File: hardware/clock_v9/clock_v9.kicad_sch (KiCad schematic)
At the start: 173 parts, among them J1 RJ45, J12 Conn_01x06, J14 DC-063-25A, J2 Conn_01x06_Pin, J4 USB_C_Receptacle, J5 Conn_01x06_Pin, J6 Conn_01x04_Pin, J8 Conn_01x02, Q1 2N7002, Q10 2N7002, Q2 S8550, Q3 S8050, Q4 S8050, Q5 S8050, Q9 2N7002, SW1 LC1258OASP, U1 ADA4807-1, U10 STM32F405RGTx, U11 AMS1117-3.3, U12 BA50DD0WHFP-TR, U13 M24C02-RMN, U14 CH340C, U15 USBLC6-2P6, U16 TLV3603DCKR, U17 SN74LVC1G14DBV, U2 SN74LVC1G14DBV, U3 SN74LVC1G14DBV, U4 ADA4807-1, U5 ADA4807-1, U6 TLV3603DCKR, U7 SN74LVC1G14DBV, U8 TLV3603DCKR, U9 L78L05_SOT89, Y1 AOCJY4A-10.000MHZ-SW, Y2 16MHz

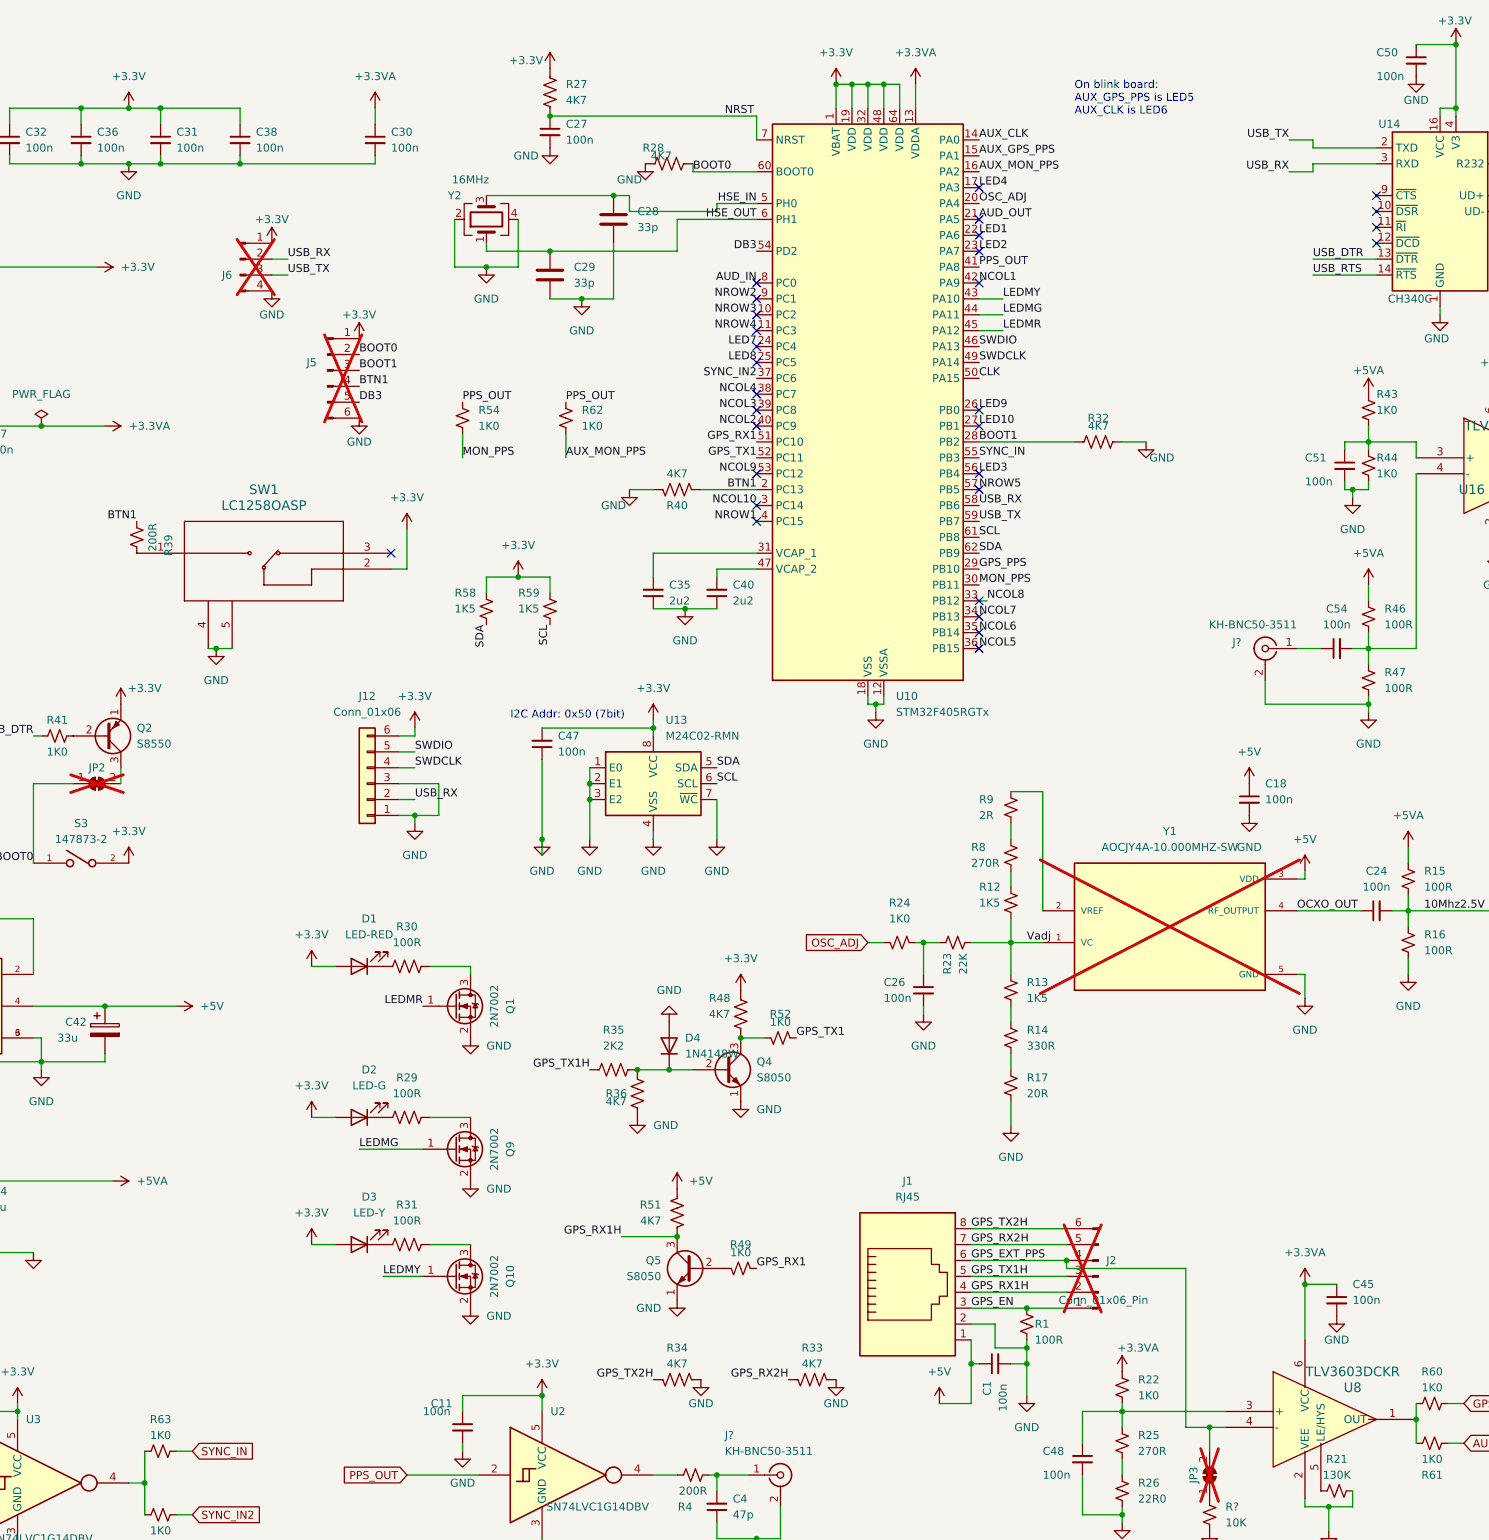
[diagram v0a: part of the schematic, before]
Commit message: add protection on inputs flips to outputs
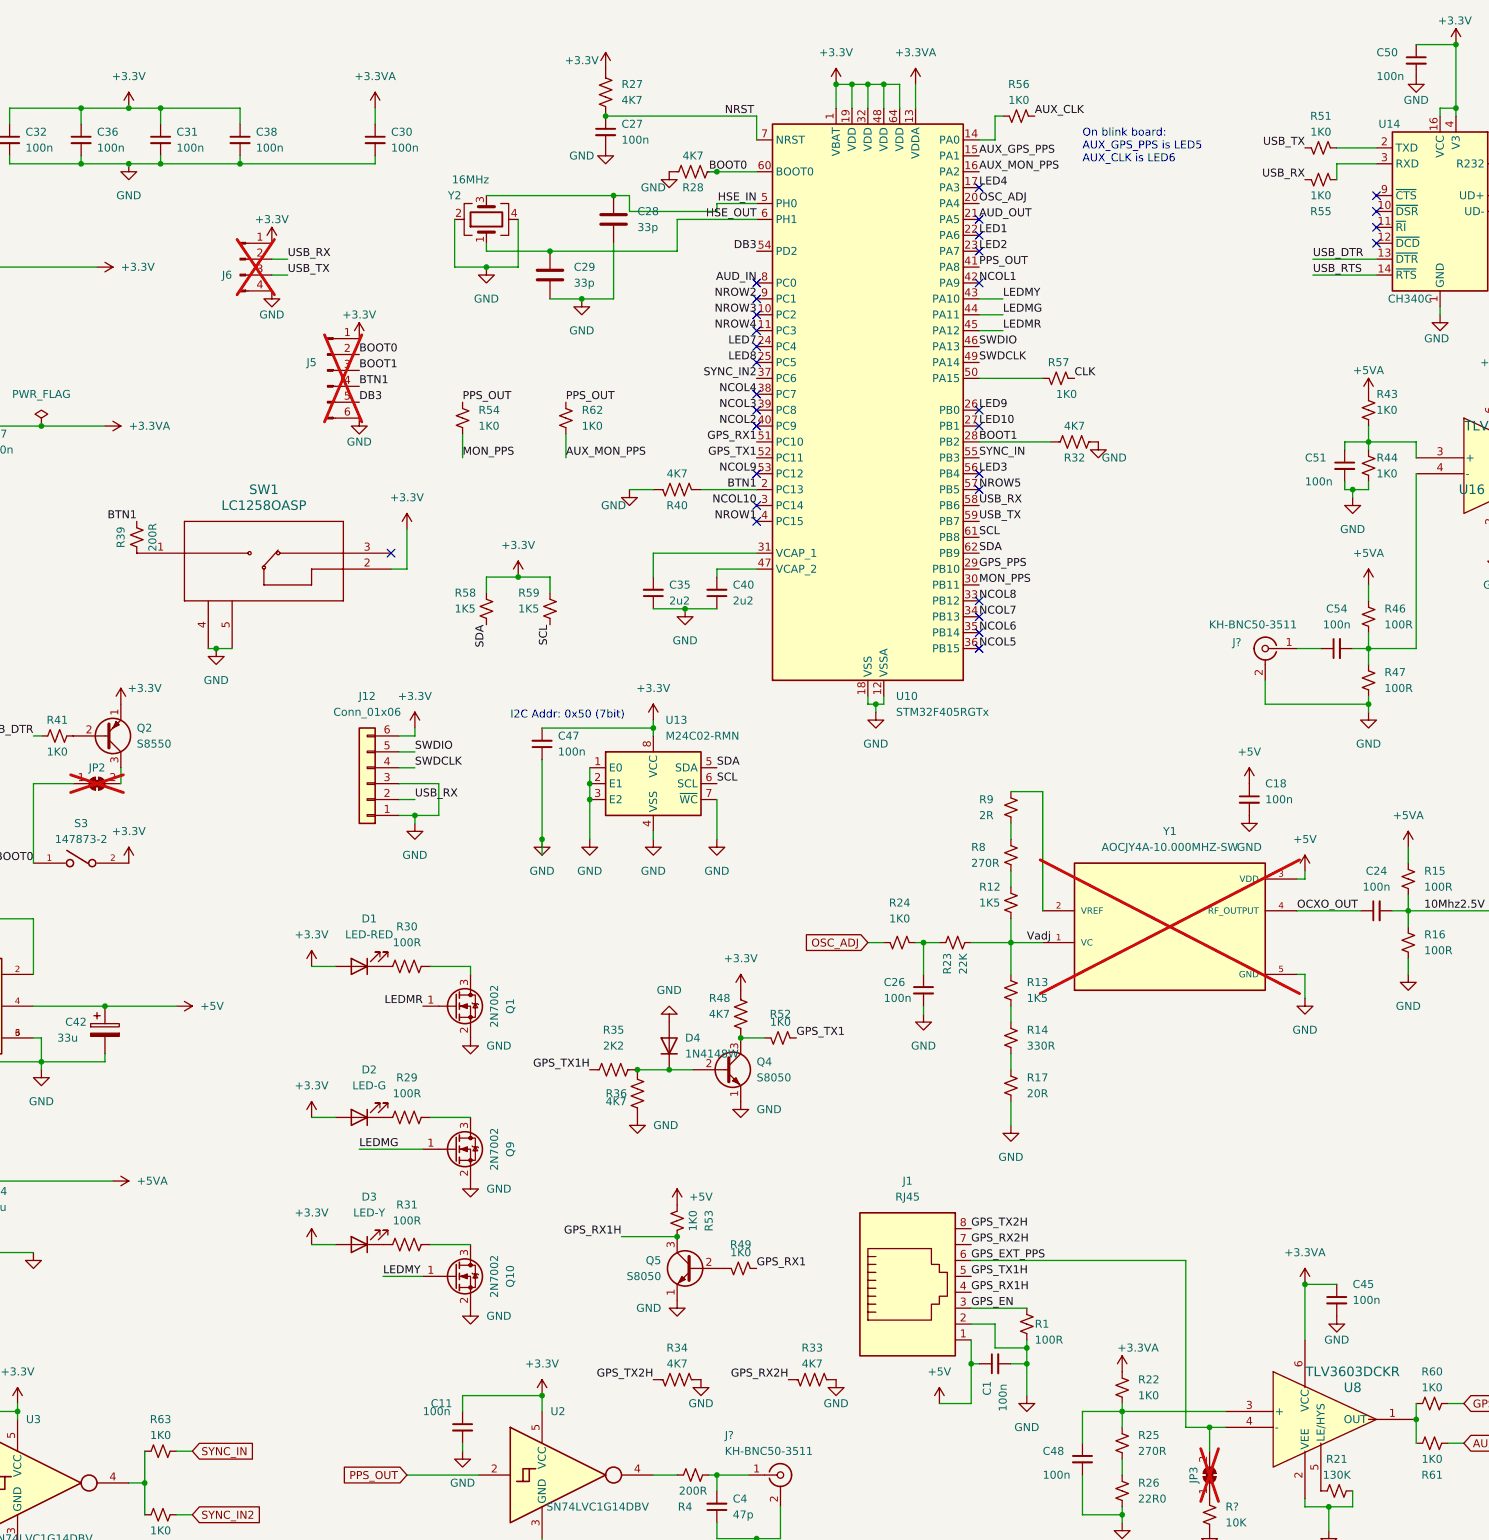
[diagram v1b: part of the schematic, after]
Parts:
- removed J2: Conn_01x06_Pin, Connector_PinHeader_2.54mm:PinHeader_1x06_P2.54mm_Vertical, symbol Connector:Conn_01x06_Pin
- removed R51: 4K7, Resistor_SMD:R_0603_1608Metric, symbol Device:R_US
- added R51, R53, R55, R56, R57: 1K0, Resistor_SMD:R_0603_1608Metric, symbol Device:R_Small_US
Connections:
- net +5V: now also R53.2
- net AUX_CLK: now also R56.1; no longer U10.14 (PA0)
- net CLK: now also R57.1; no longer U10.50 (PA15)
- net GPS_RX1H: now also R53.1
- net USB_RX: now also R55.1; no longer U14.3 (RXD)
- net USB_TX: now also R51.2; no longer U14.2 (TXD)
- new net: R56.2, U10.14 (PA0)
- new net: R57.2, U10.50 (PA15)
- new net: R51.1, U14.2 (TXD)
- new net: R55.2, U14.3 (RXD)
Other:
- moved on the sheet: C27, R27, R28, R32

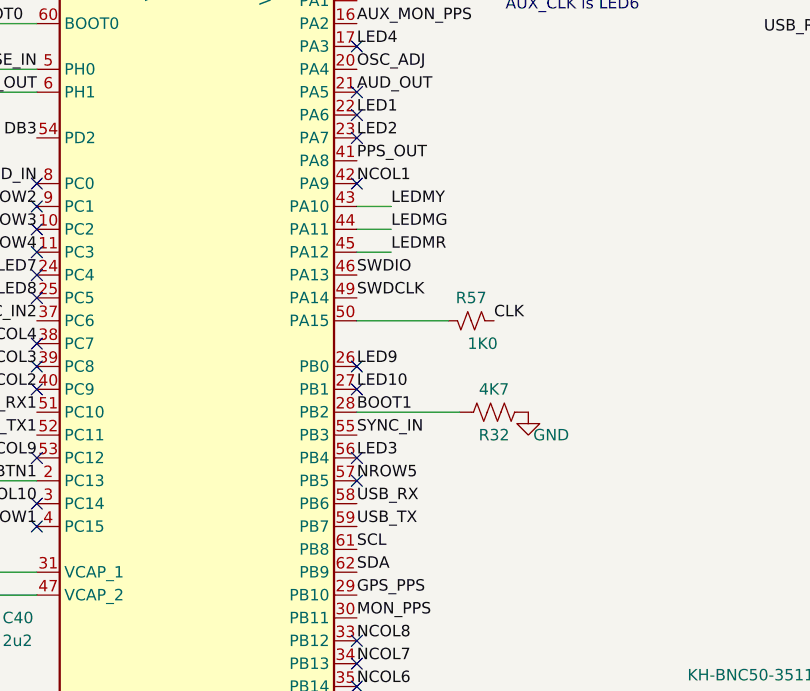
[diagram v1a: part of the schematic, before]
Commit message: move usb rx/tx on clock
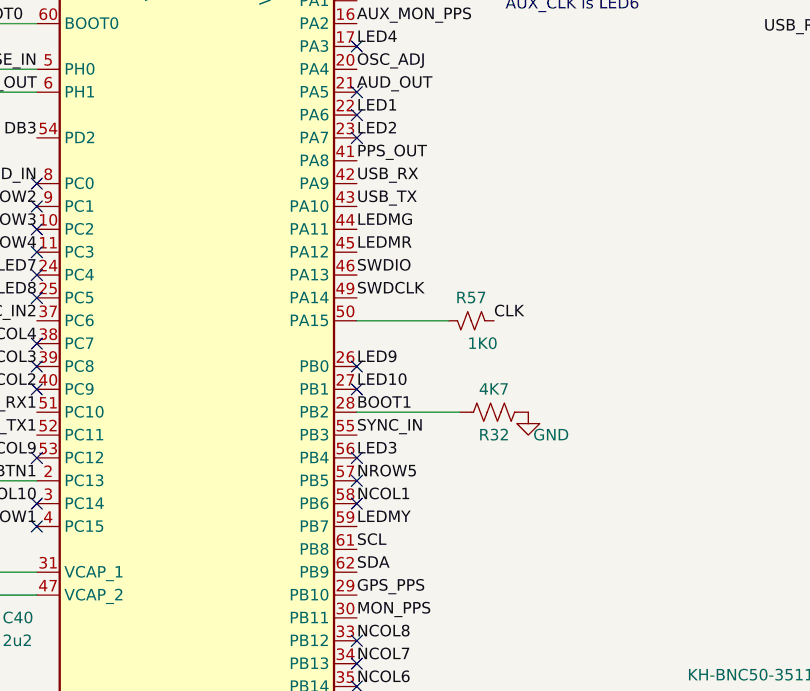
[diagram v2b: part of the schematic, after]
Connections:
- net LEDMY: now also U10.59 (PB7); no longer U10.43 (PA10)
- net NCOL1: now also U10.58 (PB6); no longer U10.42 (PA9)
- net USB_RX: now also U10.42 (PA9); no longer U10.58 (PB6)
- net USB_TX: now also U10.43 (PA10); no longer U10.59 (PB7)
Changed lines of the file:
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@@
   (no_connect (at 213.36 86.36))
   (no_connect (at 38.1 105.41))
+  (no_connect (at 213.36 91.44))
   (no_connect (at 410.21 31.75))
   (no_connect (at 276.86 44.45))
@@
   (no_connect (at 213.36 111.76))
   (no_connect (at 297.18 36.83))
-  (no_connect (at 213.36 55.88))
   (no_connect (at 177.8 93.98))
   (no_connect (at 177.8 55.88))
@@
     (stroke (width 0) (type default))
   )
-  (wire (pts (xy 217.17 60.96) (xy 213.36 60.96))
-    (stroke (width 0) (type default))
-  )
   (wire (pts (xy 69.85 27.94) (xy 77.47 27.94))
     (stroke (width 0) (type default))
@@
     (stroke (width 0) (type default))
   )
-  (wire (pts (xy 217.17 63.5) (xy 213.36 63.5))
-    (stroke (width 0) (type default))
-  )
   (wire (pts (xy 134.62 53.34) (xy 139.7 53.34))
     (stroke (width 0) (type default))
@@
   )
   (wire (pts (xy 198.12 24.13) (xy 198.12 27.94))
-    (stroke (width 0) (type default))
-  )
-  (wire (pts (xy 217.17 58.42) (xy 213.36 58.42))
     (stroke (width 0) (type default))
   )
@@
     (effects (font (size 1.27 1.27)) (justify left bottom))
   )
+  (label "LEDMY" (at 213.36 93.98 0) (fields_autoplaced)
+    (effects (font (size 1.27 1.27)) (justify left bottom))
+  )
   (label "GPS_RX1H" (at 156.21 208.28 180) (fields_autoplaced)
     (effects (font (size 1.27 1.27)) (justify right bottom))
@@
     (effects (font (size 1.27 1.27)) (justify right bottom))
   )
-  (label "LEDMY" (at 217.17 58.42 0) (fields_autoplaced)
-    (effects (font (size 1.27 1.27)) (justify left bottom))
-  )
   (label "GPS_RX2H" (at 182.88 231.14 180) (fields_autoplaced)
     (effects (font (size 1.27 1.27)) (justify right bottom))
@@
     (effects (font (size 1.27 1.27)) (justify left bottom))
   )
-  (label "LEDMR" (at 217.17 63.5 0) (fields_autoplaced)
+  (label "LEDMR" (at 213.36 63.5 0) (fields_autoplaced)
     (effects (font (size 1.27 1.27)) (justify left bottom))
   )
@@
     (effects (font (size 1.27 1.27)) (justify left bottom))
   )
-  (label "USB_TX" (at 213.36 93.98 0) (fields_autoplaced)
+  (label "USB_TX" (at 213.36 58.42 0) (fields_autoplaced)
     (effects (font (size 1.27 1.27)) (justify left bottom))
   )
@@
     (effects (font (size 1.27 1.27)) (justify left bottom))
   )
+  (label "NCOL1" (at 213.36 91.44 0) (fields_autoplaced)
+    (effects (font (size 1.27 1.27)) (justify left bottom))
+  )
   (label "NCOL5" (at 213.36 114.3 0) (fields_autoplaced)
     (effects (font (size 1.27 1.27)) (justify left bottom))
@@
     (effects (font (size 1.27 1.27)) (justify left bottom))
   )
-  (label "LEDMG" (at 217.17 60.96 0) (fields_autoplaced)
+  (label "LEDMG" (at 213.36 60.96 0) (fields_autoplaced)
     (effects (font (size 1.27 1.27)) (justify left bottom))
   )
@@
     (effects (font (size 1.27 1.27)) (justify left bottom))
   )
-  (label "USB_RX" (at 213.36 91.44 0) (fields_autoplaced)
-    (effects (font (size 1.27 1.27)) (justify left bottom))
-  )
   (label "AUD_IN" (at 177.8 55.88 180) (fields_autoplaced)
     (effects (font (size 1.27 1.27)) (justify right bottom))
@@
     (effects (font (size 1.27 1.27)) (justify left bottom))
   )
-  (label "NCOL1" (at 213.36 55.88 0) (fields_autoplaced)
-    (effects (font (size 1.27 1.27)) (justify left bottom))
-  )
   (label "SWDCLK" (at 123.19 133.35 0) (fields_autoplaced)
     (effects (font (size 1.27 1.27)) (justify left bottom))
@@
     (effects (font (size 1.27 1.27)) (justify left bottom))
   )
+  (label "USB_RX" (at 213.36 55.88 0) (fields_autoplaced)
+    (effects (font (size 1.27 1.27)) (justify left bottom))
+  )

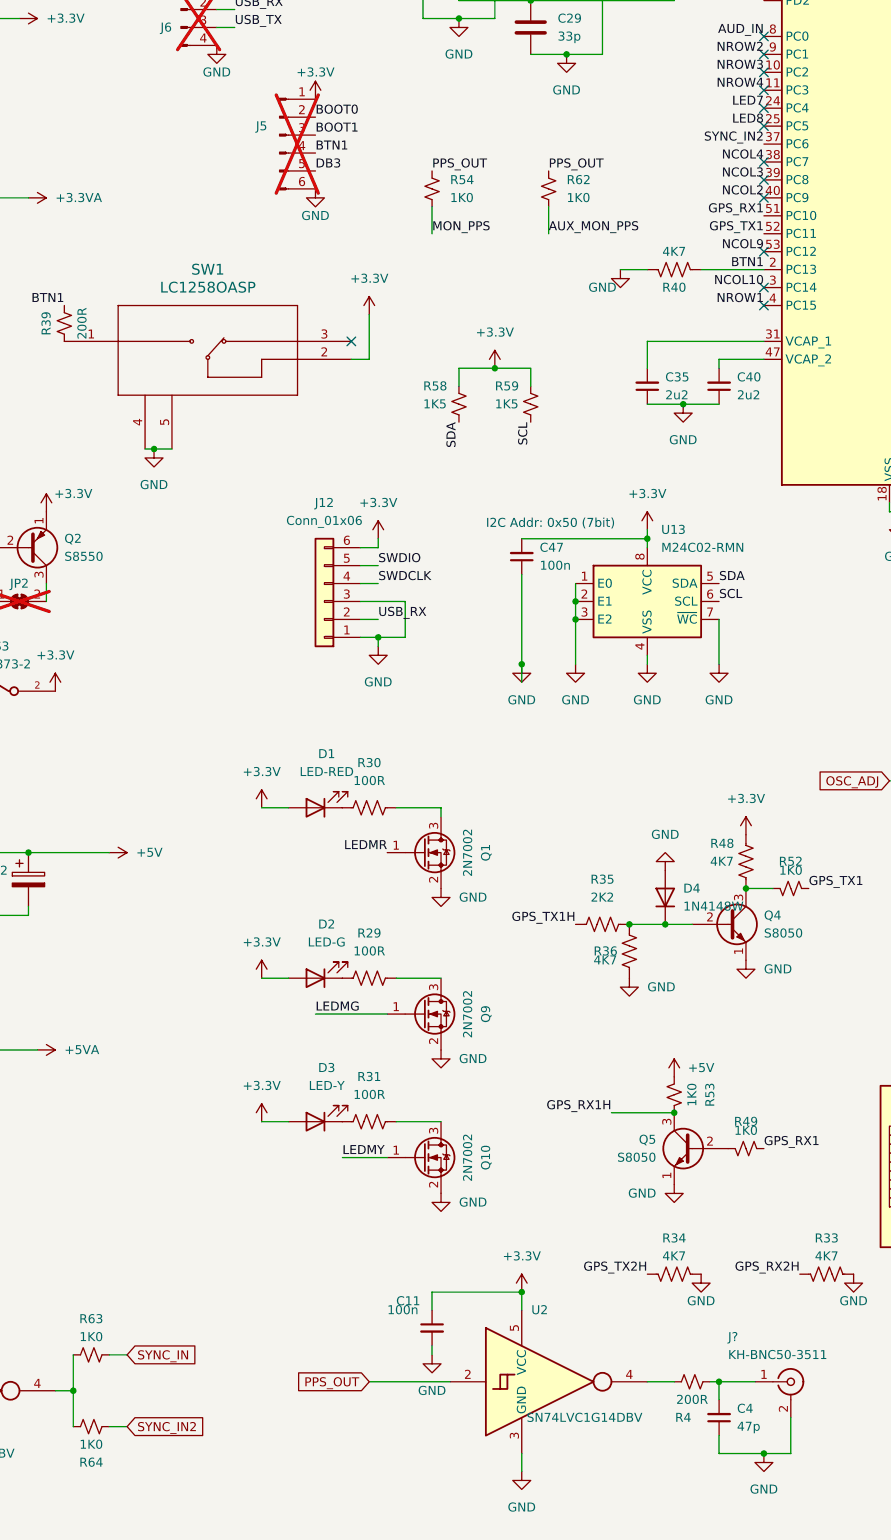
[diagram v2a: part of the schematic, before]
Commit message: rename sync_in2 to aux
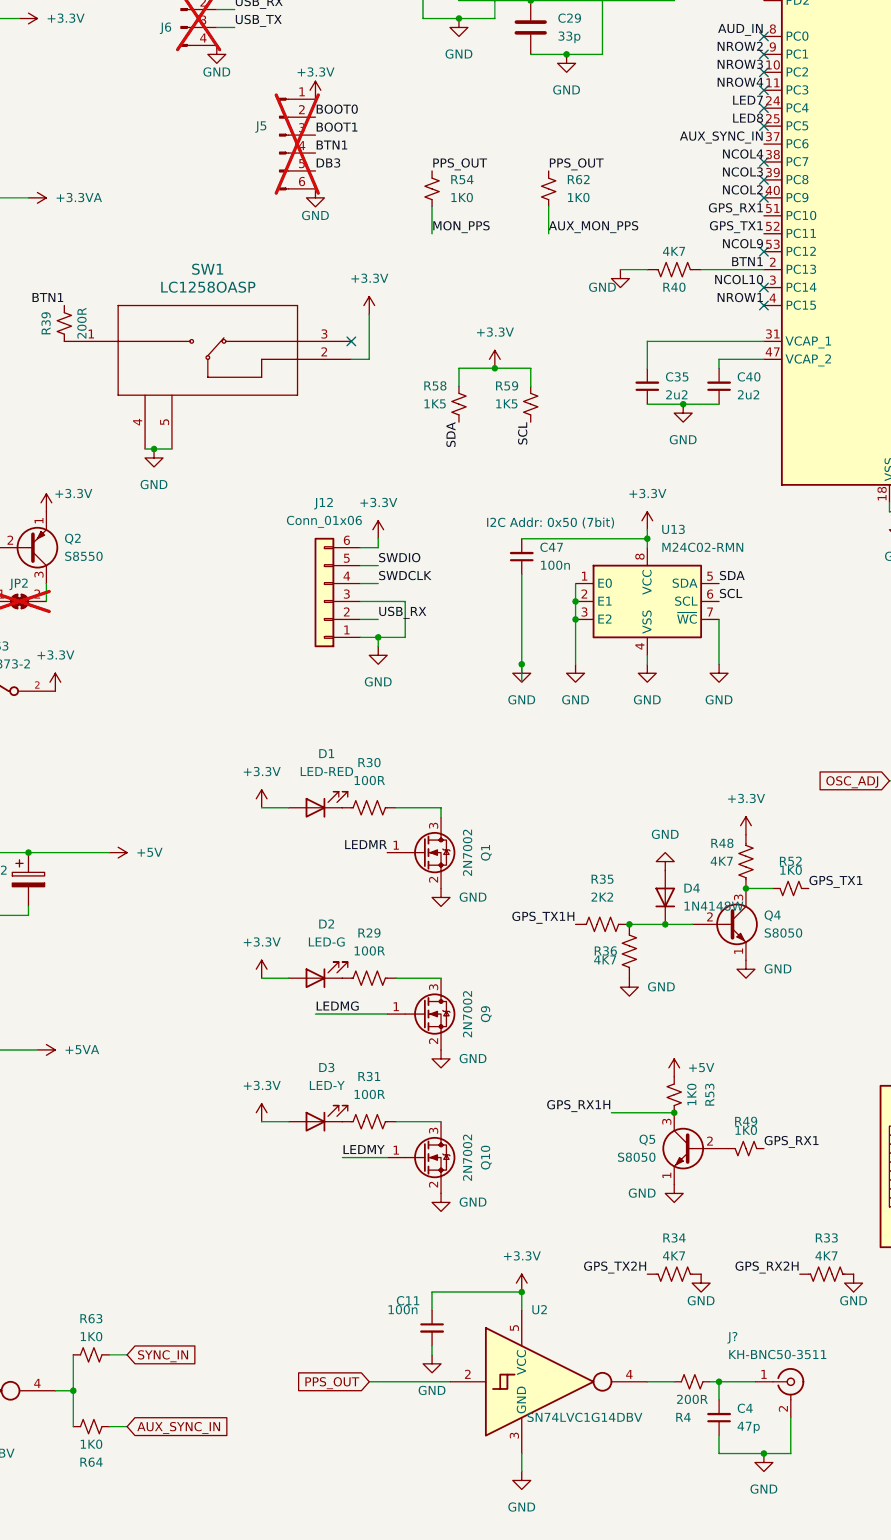
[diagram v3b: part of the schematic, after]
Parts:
- D4: JLCPCB Part # (none) -> C191023
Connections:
- net SYNC_IN2 renamed AUX_SYNC_IN
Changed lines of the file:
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@@
     (effects (font (size 1.27 1.27)) (justify left bottom))
   )
-  (label "SYNC_IN2" (at 177.8 71.12 180) (fields_autoplaced)
+  (label "AUX_SYNC_IN" (at 177.8 71.12 180) (fields_autoplaced)
     (effects (font (size 1.27 1.27)) (justify right bottom))
   )
@@
     )
   )
-  (global_label "SYNC_IN2" (shape input) (at 87.63 252.73 0) (fields_autoplaced)
+  (global_label "AUX_SYNC_IN" (shape input) (at 87.63 252.73 0) (fields_autoplaced)
     (effects (font (size 1.27 1.27)) (justify left))
     (property "Intersheetrefs" "${INTERSHEET_REFS}" (at 99.5468 252.73 0)
@@
       (effects (font (size 1.27 1.27)) hide)
     )
+    (property "JLCPCB Part #" "C191023" (at 163.83 177.8 0)
+      (effects (font (size 1.27 1.27)) hide)
+    )
